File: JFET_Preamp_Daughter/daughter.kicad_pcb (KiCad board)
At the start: 2 copper layers, 50 x 40 mm, 21 parts, among them J101 Conn_01x08_Socket, J102 Conn_01x06, J103 Conn_01x06, U101 PCM1865DBTR

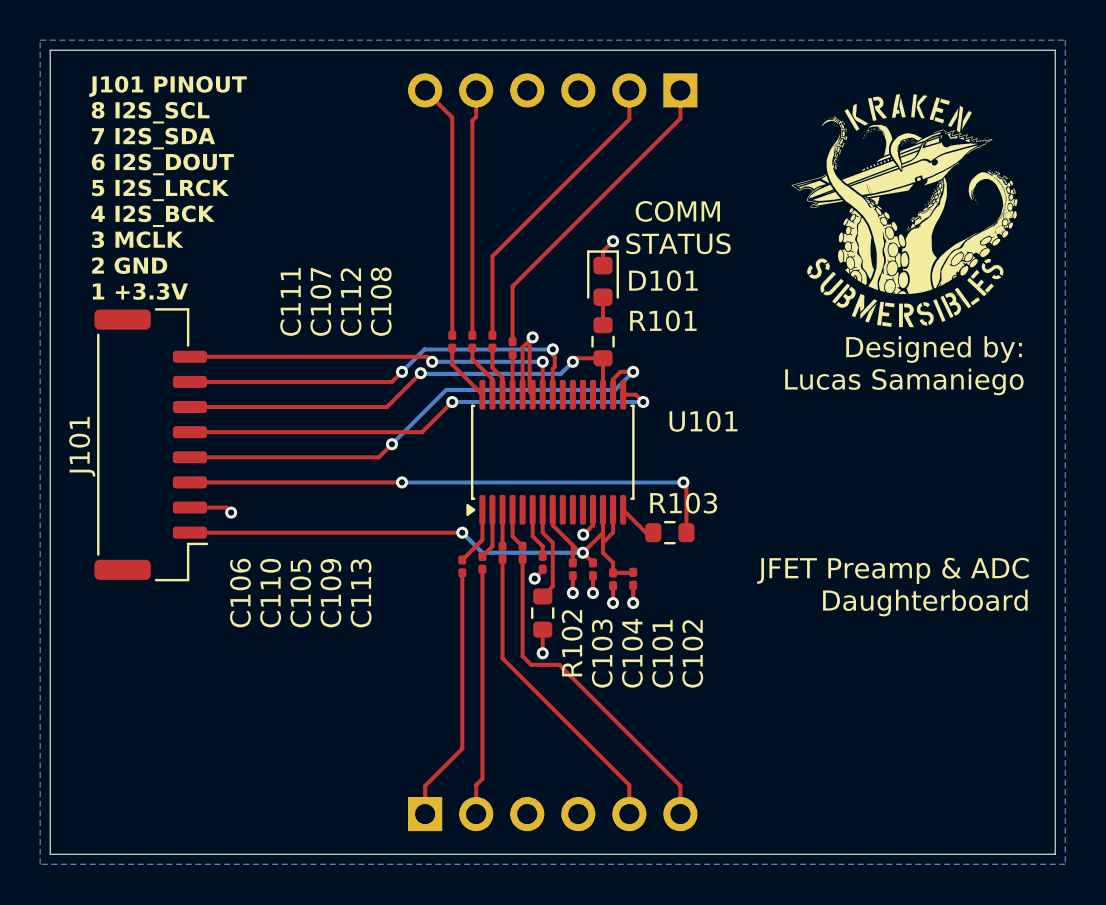
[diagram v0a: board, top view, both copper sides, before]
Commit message: update Capacitors to better suit and rebuild, prep for fab, final for 1st fab
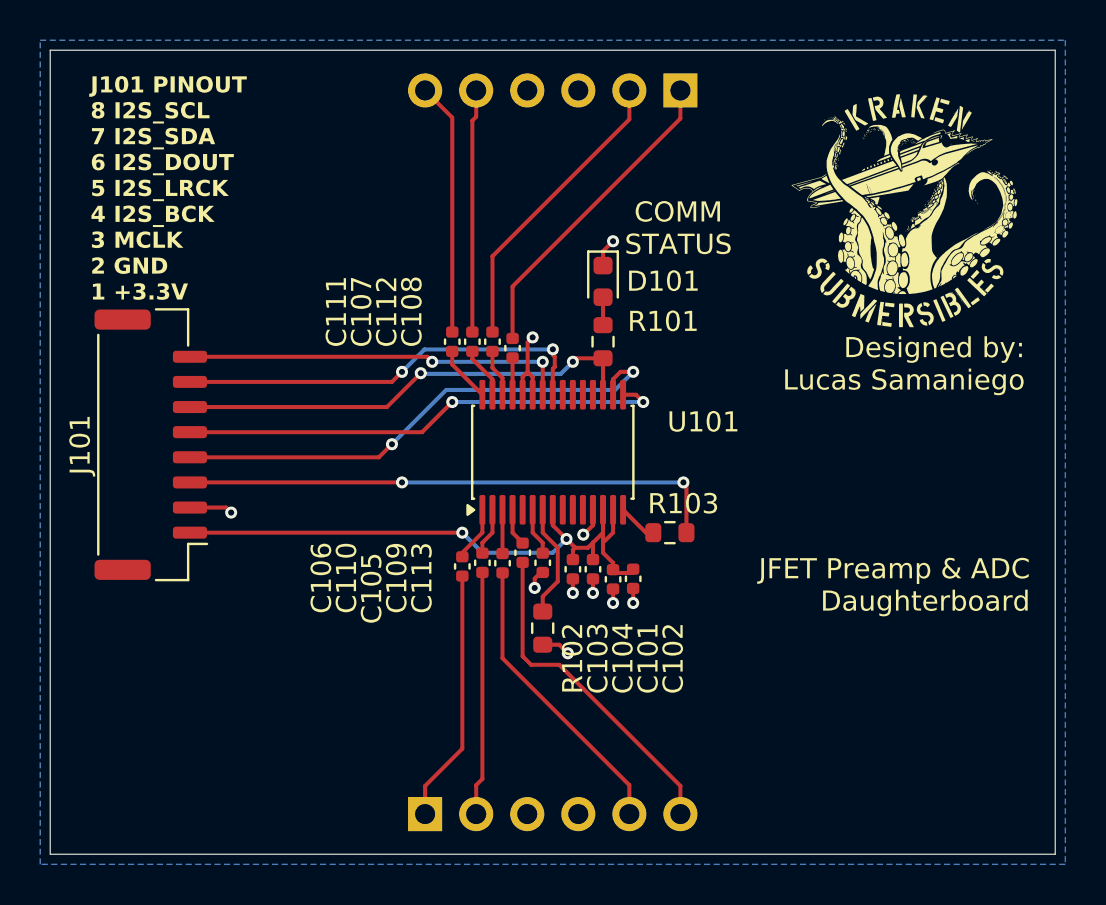
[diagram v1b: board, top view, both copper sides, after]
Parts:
- C101, C102, C103, C104, C105, C106, C107, C108, C109, C110, C111, C112, C113: footprint Capacitor_SMD:C_0201_0603Metric -> Capacitor_SMD:C_0402_1005Metric
- moved R102 0.75 mm to (49.5, 53.8)
- moved C105 0.52 mm to (47.5, 50.5)
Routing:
- net GND: track 16.3 -> 15.2 mm
- net Net-(U101-AGND): track 4.73 -> 5.68 mm
- net +3.3V: track 32.0 -> 31.2 mm
- net /CH1_HOT: track 15.3 -> 14.6 mm
